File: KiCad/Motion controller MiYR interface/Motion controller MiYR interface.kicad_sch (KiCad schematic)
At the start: 127 parts, among them CN1 Conn_02x40_Odd_Even, CN2 Conn_02x40_Odd_Even, J1 10061913-111PLF, J2 10061913-111PLF, J3 10061913-111PLF, J4 10061913-111PLF, J5 24v, M1 Fan, M2 Fan, U1 TPS54202DDC, U10 ESLC0504F, U11 ESLC0504F, U12 ESLC0504F, U13 ESLC0504F, U14 ESLC0504F, U15 ESLC0504F, U16 ESLC0504F, U17 ESLC0504F, U18 ESLC0504F, U19 ESLC0504F, U2 TPS54202DDC, U20 ESLC0504F, U21 ESLC0504F, U22 ESLC0504F, U25 TPS54202DDC, U3 ESLC0504F, U30 ESLC0504F, U31 ESLC0504F, U32 ESLC0504F, U33 ESLC0504F, U4 ESLC0504F, U5 ESLC0504F, U6 ESLC0504F, U7 ESLC0504F, U8 ESLC0504F, U9 ESLC0504F

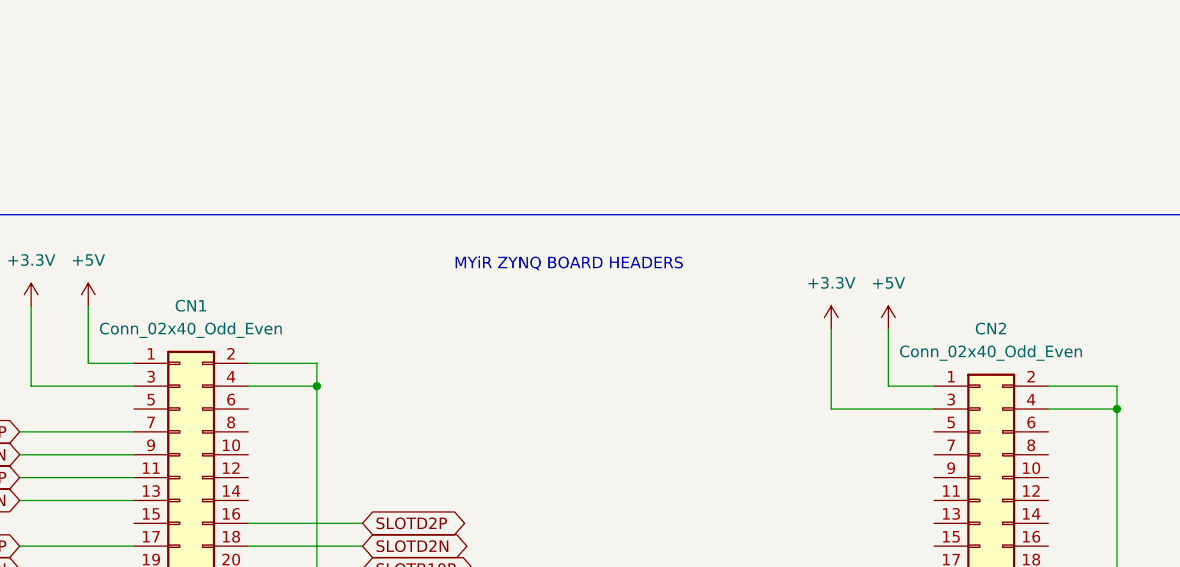
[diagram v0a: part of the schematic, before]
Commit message: add modular boards
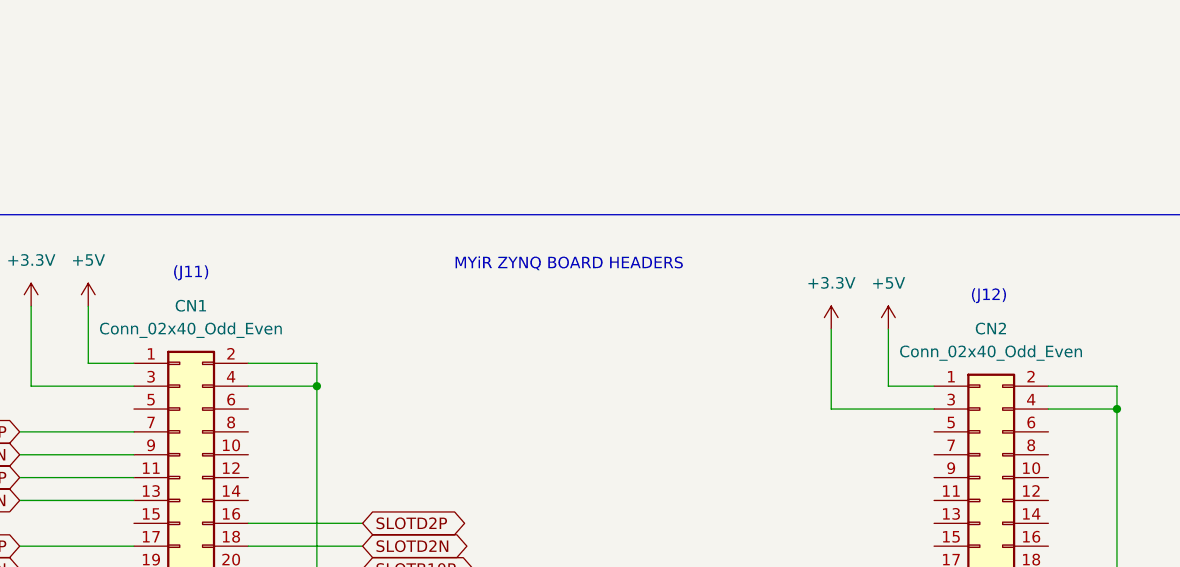
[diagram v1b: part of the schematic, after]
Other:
- note added: "(J11)"
- note added: "(J12)"
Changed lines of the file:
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@@
 		)
 	)
+	(text "(J11)"
+		(exclude_from_sim no)
+		(at 184.15 164.084 0)
+		(effects
+			(font
+				(size 1.27 1.27)
+			)
+		)
+	)
+	(text "(J12)"
+		(exclude_from_sim no)
+		(at 272.796 166.624 0)
+		(effects
+			(font
+				(size 1.27 1.27)
+			)
+		)
+	)
 	(global_label "SLOTA7P"
 		(shape bidirectional)
@@
 			(font
 				(size 1.27 1.27)
+				(color 205 205 205 1)
 			)
 			(justify right)
@@
 			(font
 				(size 1.27 1.27)
+				(color 205 205 205 1)
 			)
 			(justify right)
